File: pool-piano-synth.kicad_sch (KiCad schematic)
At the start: 15 parts, among them J2 Screw_Terminal_01x02, U2 ESP32-DevKitC, U3 Teensy4.1

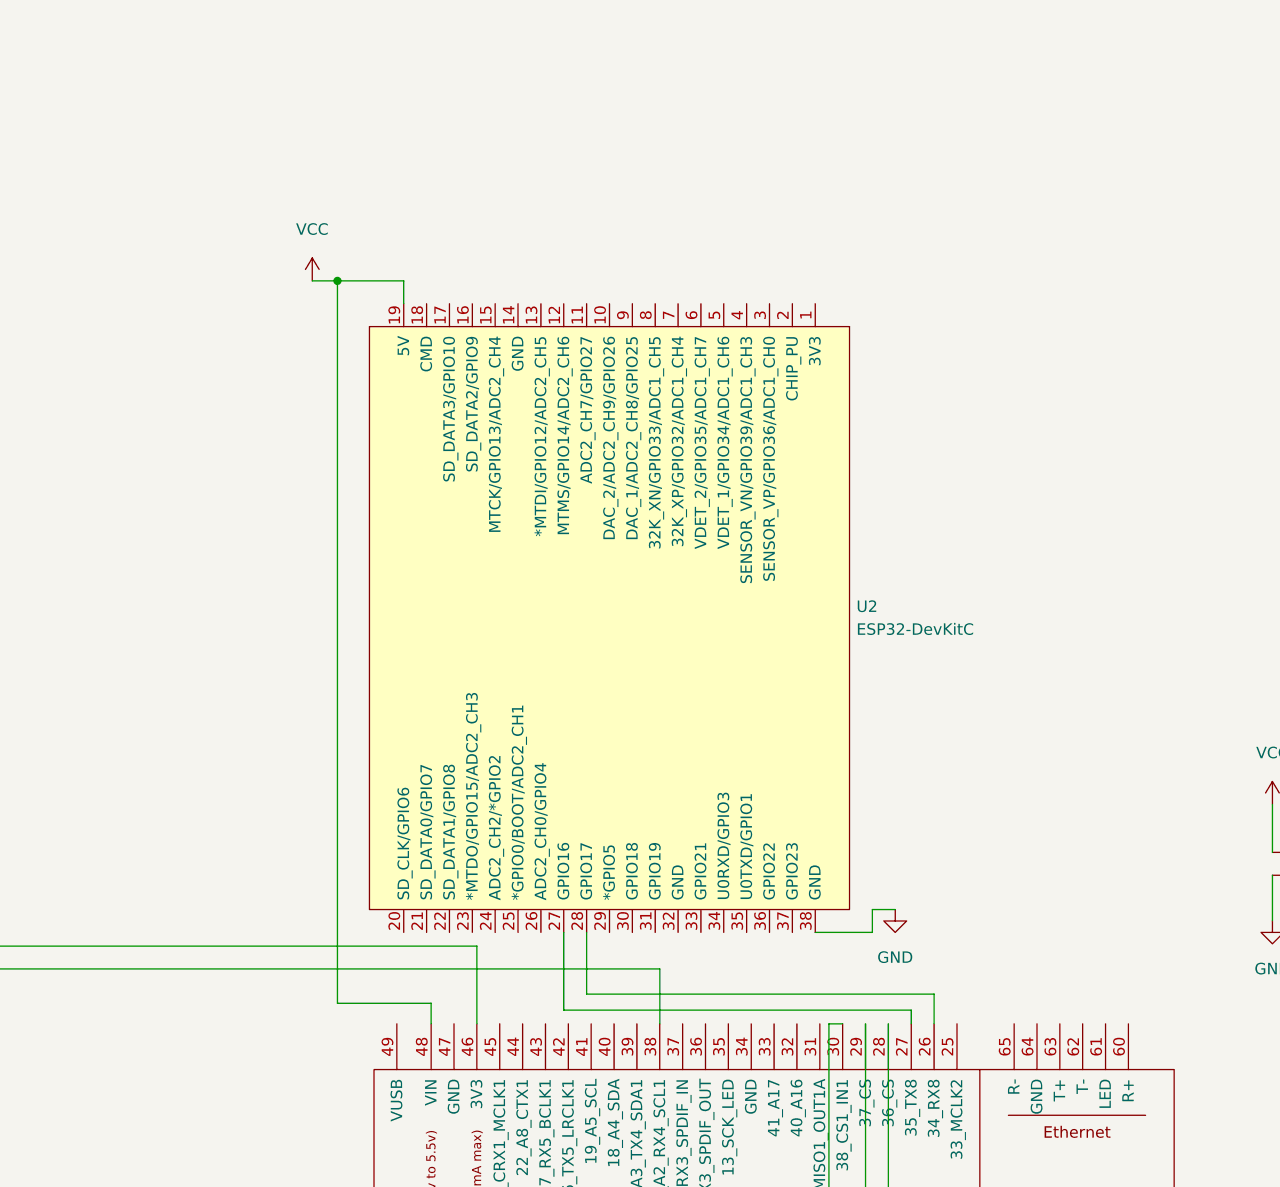
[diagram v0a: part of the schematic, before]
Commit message: v0: ready to print
- add traces, zones, better footprints
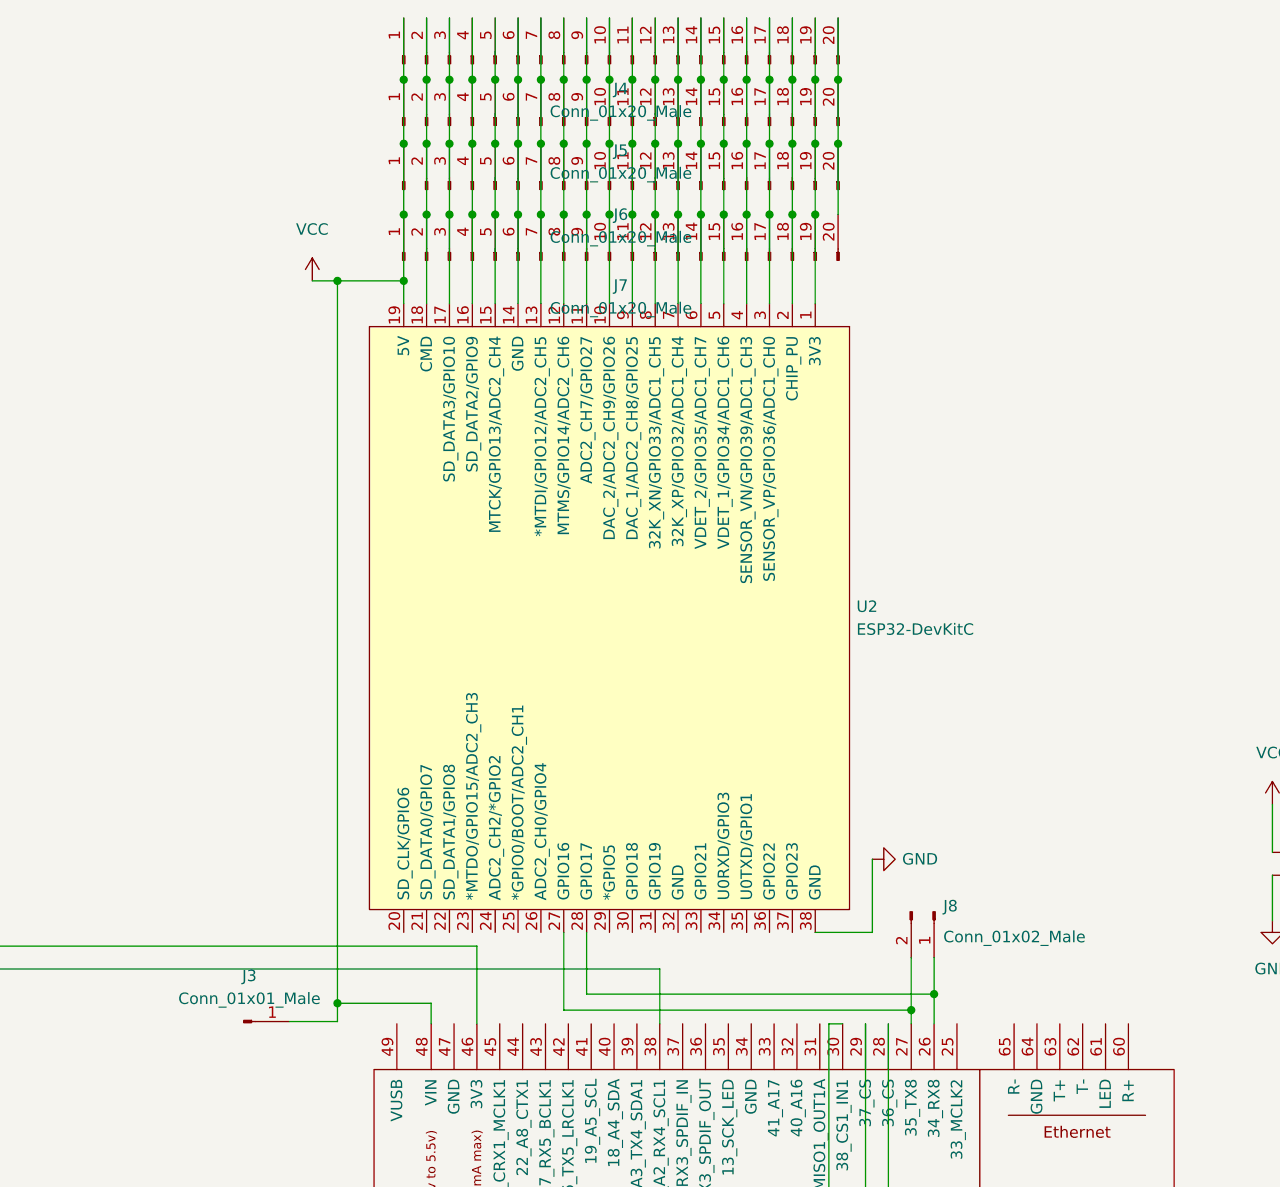
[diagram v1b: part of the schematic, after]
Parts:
- added J3: Conn_01x01_Male, Connector_PinHeader_2.54mm:PinHeader_1x01_P2.54mm_Vertical, symbol Connector:Conn_01x01_Male
- added J4, J5, J6, J7: Conn_01x20_Male, Connector_PinHeader_2.54mm:PinHeader_1x20_P2.54mm_Vertical, symbol Connector:Conn_01x20_Male
- added J8: Conn_01x02_Male, Connector_PinHeader_2.54mm:PinHeader_1x02_P2.54mm_Vertical, symbol Connector:Conn_01x02_Male
- C1: footprint Capacitor_THT:CP_Radial_D8.0mm_P5.00mm -> Capacitor_THT:CP_Radial_D10.0mm_P5.00mm
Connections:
- net VCC: now also J3.1 (Pin_1), J4.1 (Pin_1), J5.1 (Pin_1), J6.1 (Pin_1), J7.1 (Pin_1)
- net at U2.1 (3V3): now also J4.19 (Pin_19), J5.19 (Pin_19), J6.19 (Pin_19), J7.19 (Pin_19)
- net at U2.10 (DAC_2/ADC2_CH9/GPIO26): now also J4.10 (Pin_10), J5.10 (Pin_10), J6.10 (Pin_10), J7.10 (Pin_10)
- net at U2.11 (ADC2_CH7/GPIO27): now also J4.9 (Pin_9), J5.9 (Pin_9), J6.9 (Pin_9), J7.9 (Pin_9)
- net at U2.12 (MTMS/GPIO14/ADC2_CH6): now also J4.8 (Pin_8), J5.8 (Pin_8), J6.8 (Pin_8), J7.8 (Pin_8)
- net at U2.13 (*MTDI/GPIO12/ADC2_CH5): now also J4.7 (Pin_7), J5.7 (Pin_7), J6.7 (Pin_7), J7.7 (Pin_7)
- net at U2.14 (GND): now also J4.6 (Pin_6), J5.6 (Pin_6), J6.6 (Pin_6), J7.6 (Pin_6)
- net at U2.15 (MTCK/GPIO13/ADC2_CH4): now also J4.5 (Pin_5), J5.5 (Pin_5), J6.5 (Pin_5), J7.5 (Pin_5)
- net at U2.16 (SD_DATA2/GPIO9): now also J4.4 (Pin_4), J5.4 (Pin_4), J6.4 (Pin_4), J7.4 (Pin_4)
- net at U2.17 (SD_DATA3/GPIO10): now also J4.3 (Pin_3), J5.3 (Pin_3), J6.3 (Pin_3), J7.3 (Pin_3)
- net at U2.18 (CMD): now also J4.2 (Pin_2), J5.2 (Pin_2), J6.2 (Pin_2), J7.2 (Pin_2)
- net at U2.2 (CHIP_PU): now also J4.18 (Pin_18), J5.18 (Pin_18), J6.18 (Pin_18), J7.18 (Pin_18)
- net at U2.27 (GPIO16), U3.27 (35_TX8): now also J8.2 (Pin_2)
- net at U2.28 (GPIO17), U3.26 (34_RX8): now also J8.1 (Pin_1)
- net at U2.3 (SENSOR_VP/GPIO36/ADC1_CH0): now also J4.17 (Pin_17), J5.17 (Pin_17), J6.17 (Pin_17), J7.17 (Pin_17)
- net at U2.4 (SENSOR_VN/GPIO39/ADC1_CH3): now also J4.16 (Pin_16), J5.16 (Pin_16), J6.16 (Pin_16), J7.16 (Pin_16)
- net at U2.5 (VDET_1/GPIO34/ADC1_CH6): now also J4.15 (Pin_15), J5.15 (Pin_15), J6.15 (Pin_15), J7.15 (Pin_15)
- net at U2.6 (VDET_2/GPIO35/ADC1_CH7): now also J4.14 (Pin_14), J5.14 (Pin_14), J6.14 (Pin_14), J7.14 (Pin_14)
- net at U2.7 (32K_XP/GPIO32/ADC1_CH4): now also J4.13 (Pin_13), J5.13 (Pin_13), J6.13 (Pin_13), J7.13 (Pin_13)
- net at U2.8 (32K_XN/GPIO33/ADC1_CH5): now also J4.12 (Pin_12), J5.12 (Pin_12), J6.12 (Pin_12), J7.12 (Pin_12)
- net at U2.9 (DAC_1/ADC2_CH8/GPIO25): now also J4.11 (Pin_11), J5.11 (Pin_11), J6.11 (Pin_11), J7.11 (Pin_11)
- new net: J4.20 (Pin_20), J5.20 (Pin_20), J6.20 (Pin_20), J7.20 (Pin_20)
